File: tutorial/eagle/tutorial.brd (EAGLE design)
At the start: 99.1 x 73.7 mm, 16 parts, among them X2 8MHz, X4 MINI-USB

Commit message: rename pins in tutorial
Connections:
- net D10* renamed D10
- net D11* renamed D11
- net D12* renamed D12
- net D13* renamed D13
- net D5* renamed D5
- net D6* renamed D6
- net D7* renamed D7
- net D8* renamed D8
- net D9* renamed D9
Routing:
- added copper zone on layer 16, net GND
- removed copper zone on layer 1, net GND
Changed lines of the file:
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@@
 <?xml version="1.0" encoding="utf-8"?>
 <!DOCTYPE eagle SYSTEM "eagle.dtd">
-<eagle version="8.3.2">
+<eagle version="8.5.0">
 <drawing>
 <settings>
-<setting alwaysvectorfont="yes"/>
+<setting alwaysvectorfont="no"/>
 <setting keepoldvectorfont="yes"/>
 <setting verticaltext="up"/>
@@
 <param name="dpMaxLengthDifference" value="10mm"/>
 <param name="dpGapFactor" value="2.5"/>
-<param name="checkGrid" value="0"/>
 <param name="checkAngle" value="0"/>
 <param name="checkFont" value="1"/>
 <param name="checkRestrict" value="0"/>
+<param name="checkStop" value="0"/>
+<param name="checkValues" value="0"/>
 <param name="useDiameter" value="13"/>
 <param name="maxErrors" value="50"/>
@@
 <contactref element="C12" pad="1"/>
 <contactref element="C10" pad="2"/>
-<polygon width="0.4064" layer="1">
+<polygon width="0.4064" layer="16">
 <vertex x="0" y="73.66"/>
 <vertex x="0" y="0"/>
@@
 <wire x1="39.23" y1="55.965" x2="85.855" y2="45.72" width="0" layer="19" extent="1-1"/>
 </signal>
-<signal name="D11*">
+<signal name="D11">
 <contactref element="32U4" pad="12"/>
 </signal>
-<signal name="D9*">
+<signal name="D9">
 <contactref element="32U4" pad="29"/>
 </signal>
@@
 <contactref element="32U4" pad="37"/>
 </signal>
-<signal name="D5*">
+<signal name="D5">
 <contactref element="32U4" pad="31"/>
 </signal>
@@
 <wire x1="36.03" y1="55.965" x2="40.03" y2="55.965" width="0" layer="19" extent="1-1"/>
 </signal>
-<signal name="D6*">
+<signal name="D6">
 <contactref element="32U4" pad="27"/>
 </signal>
-<signal name="D10*">
+<signal name="D10">
 <contactref element="32U4" pad="30"/>
 </signal>
@@
 <contactref element="32U4" pad="20"/>
 </signal>
-<signal name="D7*">
+<signal name="D7">
 <contactref element="32U4" pad="1"/>
 </signal>
-<signal name="D13*">
+<signal name="D13">
 <contactref element="32U4" pad="32"/>
 </signal>
@@
 <contactref element="32U4" pad="36"/>
 </signal>
-<signal name="D12*">
+<signal name="D12">
 <contactref element="32U4" pad="26"/>
 </signal>
-<signal name="D8*">
+<signal name="D8">
 <contactref element="32U4" pad="28"/>
 </signal>

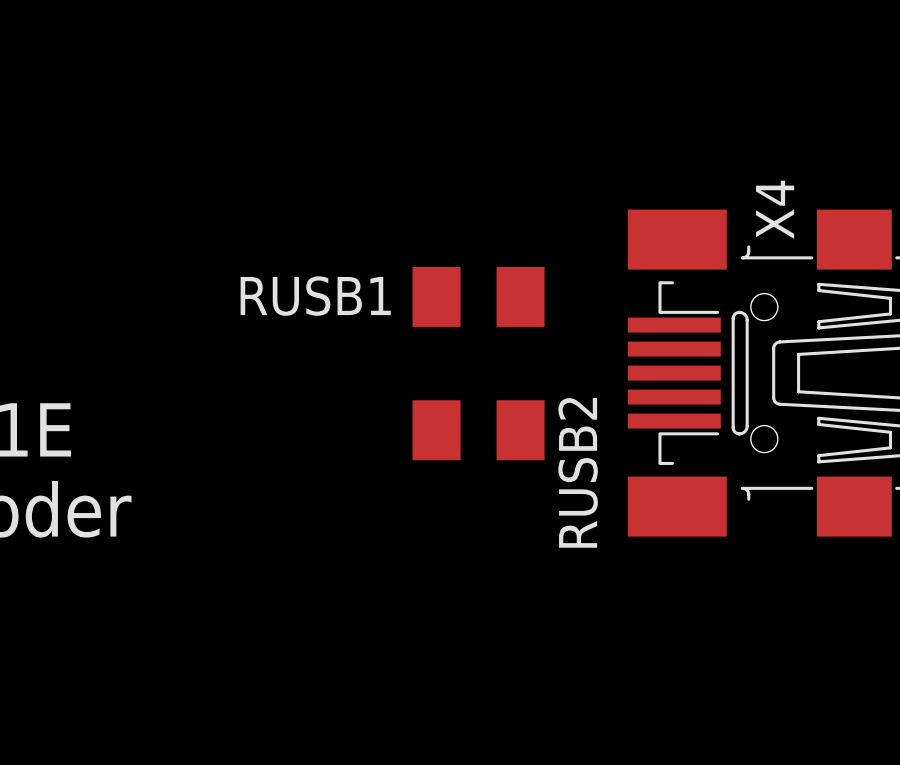
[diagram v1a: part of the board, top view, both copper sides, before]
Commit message: fix eagle demo and 22 ohms position
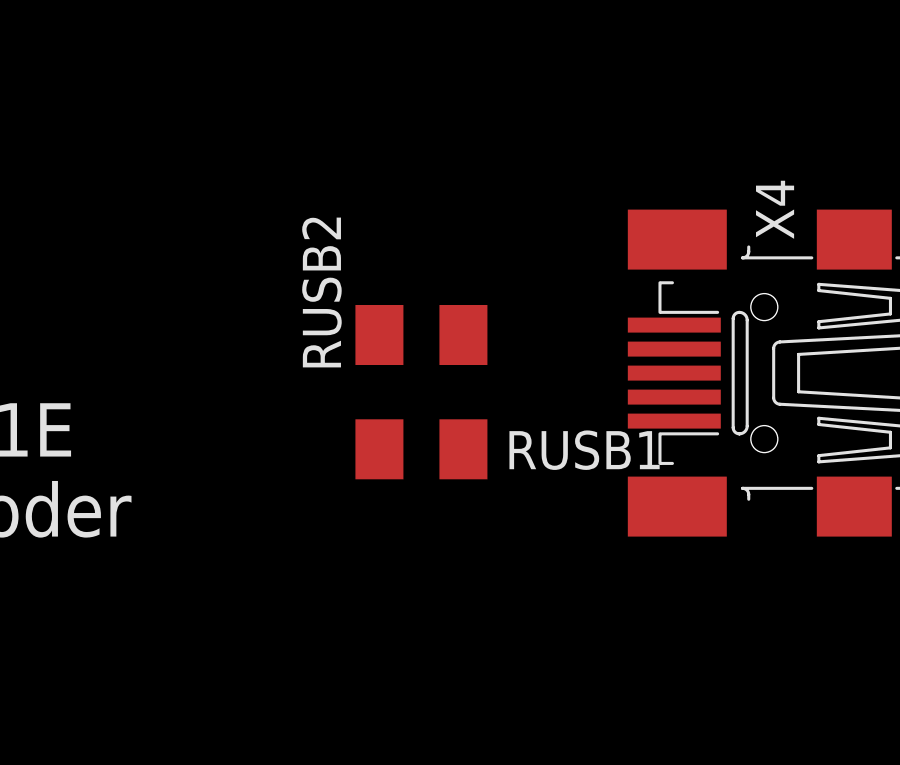
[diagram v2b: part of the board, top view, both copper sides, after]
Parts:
- moved RUSB1 5.43 mm to (82.5, 40.6), turned to 0 degrees
- moved RUSB2 3.70 mm to (82.5, 44.5), turned to 0 degrees
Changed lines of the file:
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@@
 <?xml version="1.0" encoding="utf-8"?>
 <!DOCTYPE eagle SYSTEM "eagle.dtd">
-<eagle version="8.5.0">
+<eagle version="8.6.0">
 <drawing>
 <settings>
@@
 <attribute name="VALUE" x="98.425" y="50.165" size="1.27" layer="27" rot="R180"/>
 </element>
-<element name="RUSB2" library="rcl" package="M1206" package3d_urn="urn:adsk.eagle:package:23566/1" value="22" x="84.455" y="41.275" smashed="yes" rot="R180">
-<attribute name="NAME" x="87.136890625" y="42.5091625" size="1.27" layer="25" rot="R270"/>
-<attribute name="VALUE" x="85.612709375" y="39.7712875" size="1.27" layer="27" rot="R180"/>
-</element>
-<element name="RUSB1" library="rcl" package="M1206" package3d_urn="urn:adsk.eagle:package:23566/1" value="22" x="84.455" y="45.72" smashed="yes" rot="R180">
-<attribute name="NAME" x="81.674346875" y="46.38359375" size="1.27" layer="25" rot="R180"/>
-<attribute name="VALUE" x="85.761590625" y="48.389859375" size="1.27" layer="27" rot="R180"/>
+<element name="RUSB2" library="rcl" package="M1206" package3d_urn="urn:adsk.eagle:package:23566/1" value="22" x="82.55" y="44.45" smashed="yes">
+<attribute name="NAME" x="79.868109375" y="43.2158375" size="1.27" layer="25" rot="R90"/>
+<attribute name="VALUE" x="81.392290625" y="45.9537125" size="1.27" layer="27"/>
+</element>
+<element name="RUSB1" library="rcl" package="M1206" package3d_urn="urn:adsk.eagle:package:23566/1" value="22" x="82.55" y="40.64" smashed="yes">
+<attribute name="NAME" x="85.330653125" y="39.97640625" size="1.27" layer="25"/>
+<attribute name="VALUE" x="81.243409375" y="37.970140625" size="1.27" layer="27"/>
 </element>
 <element name="C10" library="resistor" library_urn="urn:adsk.eagle:library:348" package="C1206" package3d_urn="urn:adsk.eagle:package:26140/1" value="100nF" x="49.53" y="53.34" smashed="yes">
@@
 <contactref element="RUSB1" pad="1"/>
 <contactref element="32U4" pad="3"/>
-<wire x1="39.23" y1="55.965" x2="85.855" y2="45.72" width="0" layer="19" extent="1-1"/>
+<wire x1="39.23" y1="55.965" x2="81.15" y2="40.64" width="0" layer="19" extent="1-1"/>
 </signal>
 <signal name="D11">
@@
 <contactref element="X4" pad="2"/>
 <contactref element="RUSB1" pad="2"/>
-<wire x1="83.055" y1="45.72" x2="90.98" y2="42.38" width="0" layer="19" extent="1-1"/>
+<wire x1="83.95" y1="40.64" x2="90.98" y2="42.38" width="0" layer="19" extent="1-1"/>
 </signal>
 <signal name="USBC_P">
 <contactref element="X4" pad="3"/>
 <contactref element="RUSB2" pad="2"/>
-<wire x1="83.055" y1="41.275" x2="90.98" y2="43.18" width="0" layer="19" extent="1-1"/>
+<wire x1="83.95" y1="44.45" x2="90.98" y2="43.18" width="0" layer="19" extent="1-1"/>
 </signal>
 <signal name="A0">
@@
 <contactref element="RUSB2" pad="1"/>
 <contactref element="32U4" pad="4"/>
-<wire x1="38.43" y1="55.965" x2="85.855" y2="41.275" width="0" layer="19" extent="1-1"/>
+<wire x1="38.43" y1="55.965" x2="81.15" y2="44.45" width="0" layer="19" extent="1-1"/>
 </signal>
 <signal name="ISP+5V">

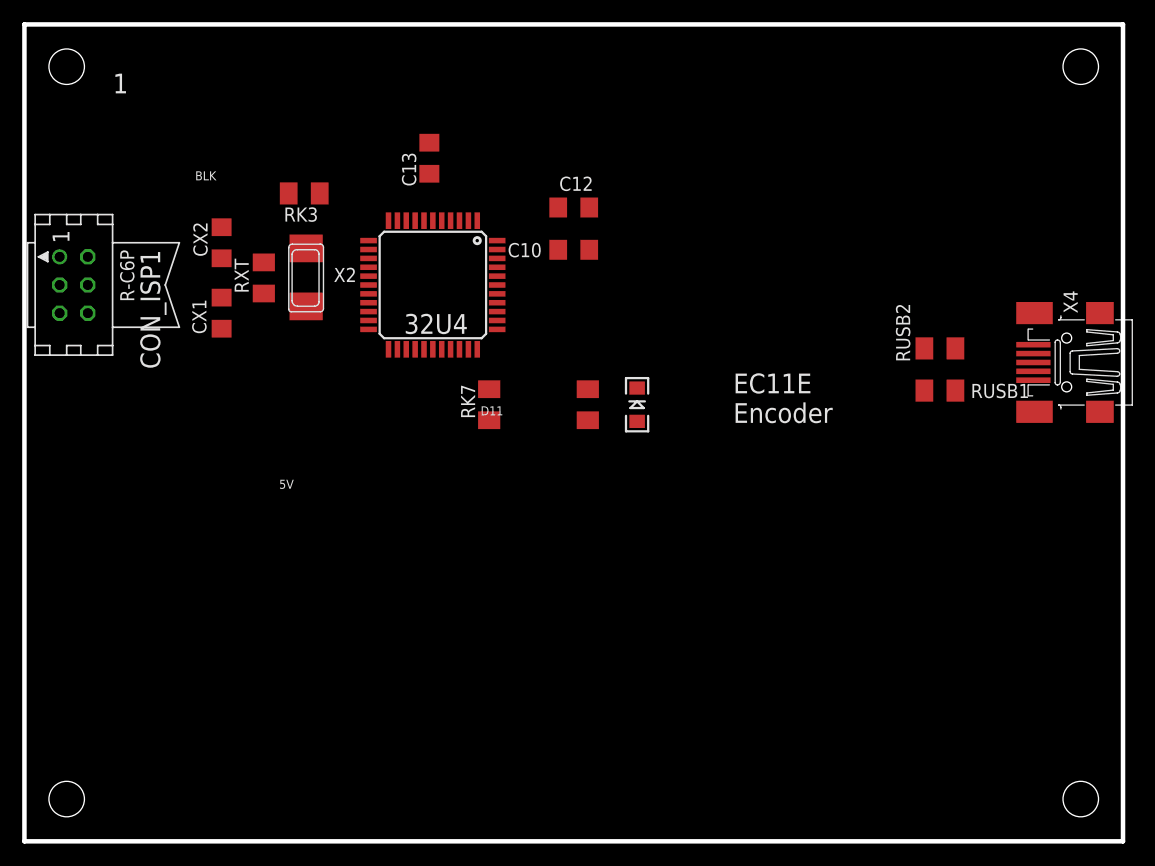
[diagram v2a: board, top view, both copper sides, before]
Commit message: update part name
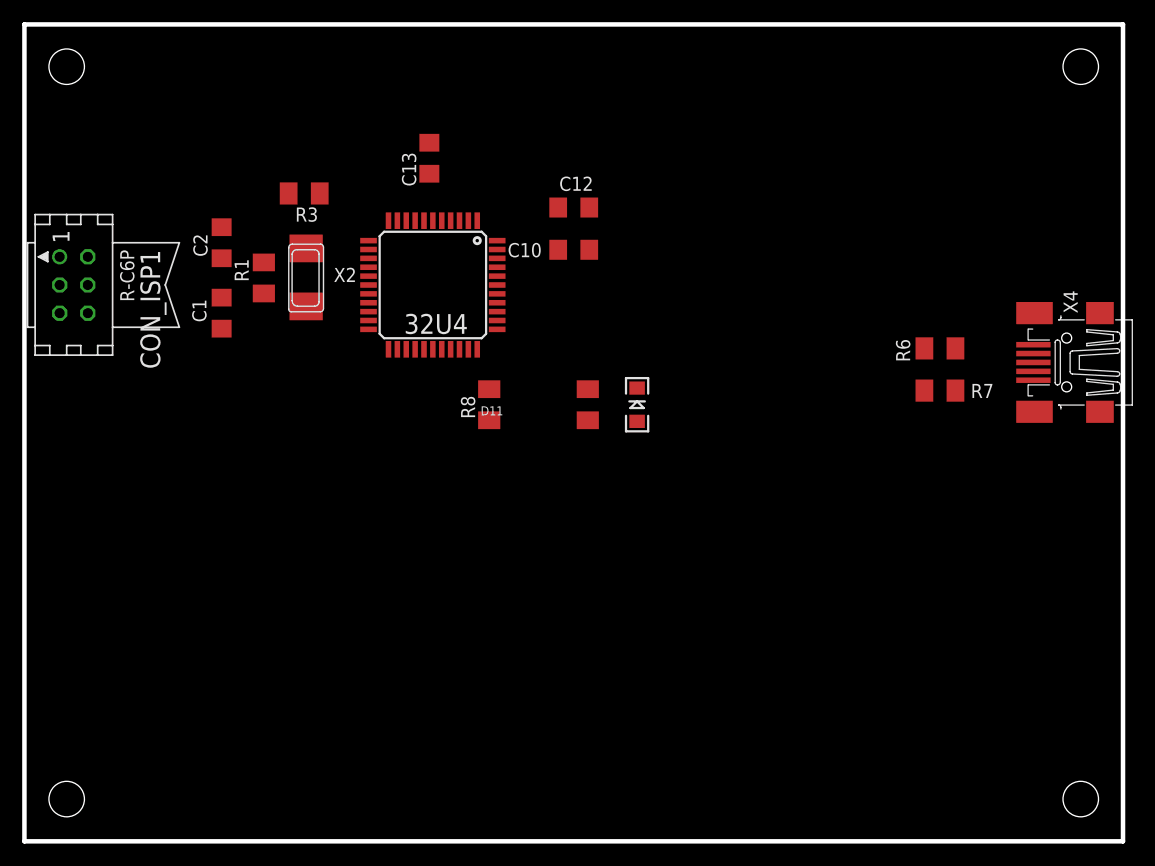
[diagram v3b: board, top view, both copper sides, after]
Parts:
- renumbered CX1 to C1, CX2 to C2, RK3 to R3, RK7 to R8, RUSB1 to R7, RUSB2 to R6, RXT to R1
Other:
- board text removed: "1"
- board text removed: "5V"
- board text removed: "BLK"
- board text removed: "Bio4_LCD_v1.1"
- board text removed: "EC11E Encoder"
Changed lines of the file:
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@@
 <layer number="23" name="tOrigins" color="15" fill="1" visible="yes" active="yes"/>
 <layer number="24" name="bOrigins" color="15" fill="1" visible="yes" active="yes"/>
-<layer number="25" name="tNames" color="7" fill="1" visible="no" active="yes"/>
-<layer number="26" name="bNames" color="7" fill="1" visible="no" active="yes"/>
+<layer number="25" name="tNames" color="7" fill="1" visible="yes" active="yes"/>
+<layer number="26" name="bNames" color="7" fill="1" visible="yes" active="yes"/>
 <layer number="27" name="tValues" color="7" fill="1" visible="yes" active="yes"/>
 <layer number="28" name="bValues" color="7" fill="1" visible="yes" active="yes"/>
@@
 <board>
 <plain>
-<text x="24.290628125" y="32.60368125" size="0.8128" layer="25" rot="R180">5V</text>
-<text x="17.296434375" y="60.41456875" size="0.8128" layer="25" rot="R180">BLK</text>
 <text x="41.1334375" y="38.41113125" size="0.8128" layer="25">D11</text>
-<text x="10.60855625" y="64.054128125" size="1.778" layer="26" rot="MR270">Bio4_LCD_v1.1</text>
-<text x="63.91295625" y="37.73088125" size="1.778" layer="25">EC11E
-Encoder</text>
-<text x="9.3588125" y="69.222134375" size="1.778" layer="25" rot="R180">1</text>
 <wire x1="0" y1="73.66" x2="0" y2="0" width="0.4064" layer="20"/>
 <wire x1="0" y1="0" x2="99.06" y2="0" width="0.4064" layer="20"/>
@@
 <attribute name="VALUE" x="52.169740625" y="40.23828125" size="1.27" layer="27" rot="R270"/>
 </element>
-<element name="X4" library="con-cypressindustries" package="32005-201" value="MINI-USB" x="93.98" y="43.18" smashed="yes" rot="R180">
+<element name="X4" library="con-cypressindustries" library_urn="urn:adsk.eagle:library:138" package="32005-201" package3d_urn="urn:adsk.eagle:package:6443/1" value="MINI-USB" x="93.98" y="43.18" smashed="yes" rot="R180">
 <attribute name="MF" value="" x="63.5" y="109.22" size="1.778" layer="27" rot="R180" display="off"/>
 <attribute name="MPN" value="" x="63.5" y="109.22" size="1.778" layer="27" rot="R180" display="off"/>
@@
 <attribute name="VALUE" x="98.425" y="50.165" size="1.27" layer="27" rot="R180"/>
 </element>
-<element name="RUSB2" library="rcl" package="M1206" package3d_urn="urn:adsk.eagle:package:23566/1" value="22" x="82.55" y="44.45" smashed="yes">
+<element name="R6" library="rcl" package="M1206" package3d_urn="urn:adsk.eagle:package:23566/1" value="22" x="82.55" y="44.45" smashed="yes">
 <attribute name="NAME" x="79.868109375" y="43.2158375" size="1.27" layer="25" rot="R90"/>
 <attribute name="VALUE" x="81.392290625" y="45.9537125" size="1.27" layer="27"/>
 </element>
-<element name="RUSB1" library="rcl" package="M1206" package3d_urn="urn:adsk.eagle:package:23566/1" value="22" x="82.55" y="40.64" smashed="yes">
+<element name="R7" library="rcl" package="M1206" package3d_urn="urn:adsk.eagle:package:23566/1" value="22" x="82.55" y="40.64" smashed="yes">
 <attribute name="NAME" x="85.330653125" y="39.97640625" size="1.27" layer="25"/>
 <attribute name="VALUE" x="81.243409375" y="37.970140625" size="1.27" layer="27"/>
@@
 <attribute name="VALUE" x="33.05353125" y="53.433190625" size="1.778" layer="27" rot="R270"/>
 </element>
-<element name="CX2" library="resistor" library_urn="urn:adsk.eagle:library:348" package="C1206" package3d_urn="urn:adsk.eagle:package:26140/1" value="22pF" x="17.78" y="53.975" smashed="yes" rot="R90">
+<element name="C2" library="resistor" library_urn="urn:adsk.eagle:library:348" package="C1206" package3d_urn="urn:adsk.eagle:package:26140/1" value="22pF" x="17.78" y="53.975" smashed="yes" rot="R90">
 <attribute name="NAME" x="16.51" y="52.705" size="1.27" layer="25" rot="R90"/>
 <attribute name="VALUE" x="20.136284375" y="52.16200625" size="1.27" layer="27" rot="R90"/>
 </element>
-<element name="CX1" library="resistor" library_urn="urn:adsk.eagle:library:348" package="C1206" package3d_urn="urn:adsk.eagle:package:26140/1" value="22pF" x="17.78" y="47.625" smashed="yes" rot="R270">
+<element name="C1" library="resistor" library_urn="urn:adsk.eagle:library:348" package="C1206" package3d_urn="urn:adsk.eagle:package:26140/1" value="22pF" x="17.78" y="47.625" smashed="yes" rot="R270">
 <attribute name="NAME" x="15.13999375" y="48.895" size="1.27" layer="25" rot="R270"/>
 <attribute name="VALUE" x="19.0164125" y="50.06428125" size="1.27" layer="27" rot="R270"/>
 </element>
-<element name="RK7" library="rcl" package="M1206" value="10k" x="41.91" y="39.37" rot="R90"/>
+<element name="R8" library="rcl" package="M1206" value="10k" x="41.91" y="39.37" rot="R90"/>
 <element name="C13" library="resistor" library_urn="urn:adsk.eagle:library:348" package="C1206" package3d_urn="urn:adsk.eagle:package:26140/1" value="100nF" x="36.5125" y="61.595" smashed="yes" rot="R270">
 <attribute name="NAME" x="35.323971875" y="59.0450125" size="1.27" layer="25" rot="R90"/>
@@
 <attribute name="VALUE" x="57.15" y="38.1" size="1.27" layer="27" rot="R180"/>
 </element>
-<element name="RXT" library="rcl" library_urn="urn:adsk.eagle:library:334" package="M1206" package3d_urn="urn:adsk.eagle:package:23566/1" value="1M" x="21.59" y="50.8" smashed="yes" rot="R270">
+<element name="R1" library="rcl" library_urn="urn:adsk.eagle:library:334" package="M1206" package3d_urn="urn:adsk.eagle:package:23566/1" value="1M" x="21.59" y="50.8" smashed="yes" rot="R270">
 <attribute name="NAME" x="18.95470625" y="52.535034375" size="1.27" layer="25" rot="R270"/>
+<attribute name="SPICEPREFIX" value="R" x="21.59" y="50.8" size="1.778" layer="27" rot="R270" display="off"/>
 <attribute name="VALUE" x="19.11484375" y="51.901834375" size="1.27" layer="27" rot="R270"/>
 </element>
-<element name="RK3" library="rcl" library_urn="urn:adsk.eagle:library:334" package="M1206" package3d_urn="urn:adsk.eagle:package:23566/1" value="10k" x="25.22855" y="58.42" rot="R180"/>
+<element name="R3" library="rcl" library_urn="urn:adsk.eagle:library:334" package="M1206" package3d_urn="urn:adsk.eagle:package:23566/1" value="10k" x="25.22855" y="58.42" rot="R180">
+<attribute name="SPICEPREFIX" value="R" x="25.22855" y="58.42" size="1.778" layer="27" rot="R180" display="off"/>
+</element>
 <element name="CON_ISP1" library="lpatiny" package="TINYISP" value="SPI" x="4.445" y="50.165" rot="R270">
 <attribute name="MF" value="" x="4.445" y="50.165" size="1.778" layer="27" rot="R270" display="off"/>
@@
 <signal name="GND" class="1">
 <contactref element="X4" pad="5"/>
-<contactref element="CX1" pad="1"/>
-<contactref element="CX2" pad="1"/>
+<contactref element="C1" pad="1"/>
+<contactref element="C2" pad="1"/>
 <contactref element="C13" pad="1"/>
 <contactref element="32U4" pad="23"/>
 <contactref element="32U4" pad="15"/>
 <contactref element="32U4" pad="5"/>
-<contactref element="RK7" pad="1"/>
+<contactref element="R8" pad="1"/>
 <contactref element="LDPW5" pad="C"/>
 <contactref element="32U4" pad="35"/>
@@
 </signal>
 <signal name="USB_N">
-<contactref element="RUSB1" pad="1"/>
+<contactref element="R7" pad="1"/>
 <contactref element="32U4" pad="3"/>
 <wire x1="39.23" y1="55.965" x2="81.15" y2="40.64" width="0" layer="19" extent="1-1"/>
@@
 <signal name="USBC_N">
 <contactref element="X4" pad="2"/>
-<contactref element="RUSB1" pad="2"/>
+<contactref element="R7" pad="2"/>
 <wire x1="83.95" y1="40.64" x2="90.98" y2="42.38" width="0" layer="19" extent="1-1"/>
 </signal>
 <signal name="USBC_P">
 <contactref element="X4" pad="3"/>
-<contactref element="RUSB2" pad="2"/>
+<contactref element="R6" pad="2"/>
 <wire x1="83.95" y1="44.45" x2="90.98" y2="43.18" width="0" layer="19" extent="1-1"/>
 </signal>
@@
 </signal>
 <signal name="RESET">
-<contactref element="RK3" pad="1"/>
+<contactref element="R3" pad="1"/>
 <contactref element="32U4" pad="13"/>
 <contactref element="CON_ISP1" pad="RESET"/>
@@
 </signal>
 <signal name="XTAL1">
-<contactref element="CX2" pad="2"/>
+<contactref element="C2" pad="2"/>
 <contactref element="32U4" pad="16"/>
 <contactref element="X2" pad="P$1"/>
-<contactref element="RXT" pad="1"/>
+<contactref element="R1" pad="1"/>
 <wire x1="25.4" y1="53.465" x2="31.03" y2="50.965" width="0" layer="19" extent="1-1"/>
 <wire x1="21.59" y1="52.2" x2="25.4" y2="53.465" width="0" layer="19" extent="1-1"/>
@@
 <signal name="HWB">
 <contactref element="32U4" pad="33"/>
-<contactref element="RK7" pad="2"/>
+<contactref element="R8" pad="2"/>
 <wire x1="41.91" y1="40.77" x2="40.83" y2="44.365" width="0" layer="19" extent="1-1"/>
 </signal>
 <signal name="N$42">
-<contactref element="CX1" pad="2"/>
+<contactref element="C1" pad="2"/>
 <contactref element="32U4" pad="17"/>
 <contactref element="X2" pad="P$2"/>
-<contactref element="RXT" pad="2"/>
+<contactref element="R1" pad="2"/>
 <wire x1="25.4" y1="48.235" x2="31.03" y2="50.165" width="0" layer="19" extent="1-1"/>
 <wire x1="21.59" y1="49.4" x2="25.4" y2="48.235" width="0" layer="19" extent="1-1"/>
@@
 <contactref element="C12" pad="2"/>
 <contactref element="32U4" pad="44"/>
-<contactref element="RK3" pad="2"/>
+<contactref element="R3" pad="2"/>
 <contactref element="X4" pad="1"/>
 <wire x1="50.8" y1="40.77" x2="90.98" y2="41.58" width="0" layer="19" extent="1-1"/>
@@
 </signal>
 <signal name="USB_P">
-<contactref element="RUSB2" pad="1"/>
+<contactref element="R6" pad="1"/>
 <contactref element="32U4" pad="4"/>
 <wire x1="38.43" y1="55.965" x2="81.15" y2="44.45" width="0" layer="19" extent="1-1"/>
@@
 </drawing>
 <compatibility>
-<note version="6.3" minversion="6.2.2" severity="warning">
-Since Version 6.2.2 text objects can contain more than one line,
-which will not be processed correctly with this version.
-</note>
 <note version="8.2" severity="warning">
 Since Version 8.2, EAGLE supports online libraries. The ids
